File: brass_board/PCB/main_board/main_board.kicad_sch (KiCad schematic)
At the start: 133 parts

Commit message: Added LTspice tests and fixed error on opamp. ready for routing
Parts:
- A1: value (none) -> Arduino_Nano_v3.x; footprint (none) -> Module:Arduino_Nano
- C1, C10, C11, C12, C13, C2, C3, C4, C5, C6, C7, C8, C9: value (none) -> C_Small; footprint (none) -> Capacitor_SMD:C_0603_1608Metric
- C14, C15: renamed from C?; value (none) -> 100uF; footprint (none) -> Capacitor_SMD:C_1210_3225Metric
- FB1, FB2, FB3: value (none) -> FerriteBead_Small; footprint (none) -> Resistor_SMD:R_0805_2012Metric
- J1, J15: value (none) -> Conn_POS_input_B; footprint (none) -> Connector_PinHeader_2.54mm:PinHeader_1x03_P2.54mm_Vertical
- J10, J26: value (none) -> Conn_Galvo_B; footprint (none) -> Connector_PinHeader_2.54mm:PinHeader_1x03_P2.54mm_Vertical
- J11: value (none) -> Conn_OLED; footprint (none) -> Connector_PinHeader_2.54mm:PinHeader_1x04_P2.54mm_Vertical
- J12: value (none) -> Conn_LED_CTL; footprint (none) -> Connector_PinHeader_2.54mm:PinHeader_1x02_P2.54mm_Vertical
- J13: value (none) -> Conn_Laser_Trigger; footprint (none) -> Connector_PinHeader_2.54mm:PinHeader_1x02_P2.54mm_Vertical
- J14, J2: value (none) -> Conn_POS_input_A; footprint (none) -> Connector_PinHeader_2.54mm:PinHeader_1x03_P2.54mm_Vertical
- J16, J17, J18, J21, J23, J24: value (none) -> Conn_02x02_Odd_Even; footprint (none) -> Connector_PinHeader_2.54mm:PinHeader_2x02_P2.54mm_Vertical
- J19: value (none) -> Conn_ADC; footprint (none) -> Connector_PinHeader_2.54mm:PinHeader_1x04_P2.54mm_Vertical
- J20, J6: value (none) -> Conn_DAC; footprint (none) -> Connector_PinHeader_2.54mm:PinHeader_1x03_P2.54mm_Vertical
- J22, J8: value (none) -> Conn_01x03_Male_Power; footprint (none) -> Connector_PinHeader_2.54mm:PinHeader_1x03_P2.54mm_Vertical
- J25, J9: value (none) -> Conn_Galvo_A; footprint (none) -> Connector_PinHeader_2.54mm:PinHeader_1x03_P2.54mm_Vertical
- J27, J3: value (none) -> Conn_01x40_Male; footprint (none) -> Connector_PinHeader_2.54mm:PinHeader_2x20_P2.54mm_Vertical
- J4: value (none) -> Conn_01x04_Male; footprint (none) -> Connector_PinHeader_2.54mm:PinHeader_1x04_P2.54mm_Vertical
- J5: value (none) -> Conn_ADC; footprint (none) -> Connector_PinHeader_2.54mm:PinHeader_2x02_P2.54mm_Vertical
- J7: value (none) -> Conn_LED_PWM; footprint (none) -> Connector_PinHeader_2.54mm:PinHeader_1x02_P2.54mm_Vertical
- Q1, Q2: value (none) -> MMBT3904; footprint (none) -> Package_TO_SOT_SMD:SOT-23
- R1, R13, R14, R2, R20, R21, R22, R23, R24, R25, R26, R27, R28, R29, R3, R30, R31, R32, R33, R34, R35, R36, R37, R4, R5, R6, R7, R8: value (none) -> 1k; footprint (none) -> Resistor_SMD:R_0603_1608Metric
- R10, R11, R12, R16, R17, R18, R19, R9: value (none) -> 12k; footprint (none) -> Resistor_SMD:R_0603_1608Metric
- R15: value (none) -> 5k; footprint (none) -> Resistor_SMD:R_0603_1608Metric
- R38, R39, R40, R41, R42, R43, R44, R45, R46, R47: value (none) -> R_Small_US; footprint (none) -> Resistor_SMD:R_0603_1608Metric
- RV1, RV10, RV11, RV12, RV2, RV3, RV4, RV5, RV6, RV7, RV8, RV9: value (none) -> 50k; footprint (none) -> Potentiometer_THT:Potentiometer_Bourns_3296W_Vertical
- TP1, TP2, TP3, TP4, TP5: value (none) -> TestPoint; footprint (none) -> Connector_PinHeader_2.54mm:PinHeader_1x01_P2.54mm_Vertical
- U1, U14, U2, U3, U4, U5, U6, U7: value (none) -> LM393; footprint (none) -> Package_SO:SOIC-8-1EP_3.9x4.9mm_P1.27mm_EP2.29x3mm
- U10, U11: value (none) -> Teensy4.0; footprint (none) -> teensy:Teensy40
- U12, U13, U15, U8, U9: value (none) -> TLV3201; footprint (none) -> Package_TO_SOT_SMD:SOT-23-5
- gave numbers to parts that had none: 6
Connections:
- net GND: now also R5.2, R7.2; no longer R6.2, R8.2
- net at R9.1, U6.1: now also R6.2; no longer R5.2
- net at R11.1, U6.7: now also R8.2; no longer R7.2
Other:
- note added: "MCU"
- moved on the sheet: A1, C1, C10, C11, C12, C13, C14, C15, C16, C17, C18, C19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

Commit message: RC1
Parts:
- removed A1: Arduino_Nano_v3.x, Module:Arduino_Nano, symbol MCU_Module:Arduino_Nano_v3.x
- removed Q1, Q2: MMBT3904, Package_TO_SOT_SMD:SOT-23, symbol Transistor_BJT:2N2219
- removed U15: TLV3201, Package_TO_SOT_SMD:SOT-23-5, symbol project:TLV3201
- added D1, D2, D3, D4, D5: (no value), symbol Device:LED
- added J28: (no value), symbol Connector:Conn_01x06_Male
- added Q1: (no value), symbol Transistor_BJT:MMBT3904
- added R56: (no value), symbol Device:R_Small_US
- added S1: (no value), symbol project:PTS525SM15SMTR2LFS
- added U15: (no value), symbol 74xx:74LS08
- added U16: (no value), symbol project:ARDUINO_PRO_MINI
- added U17: (no value), symbol project:74LVC1G34
- added U18: (no value), symbol Logic_LevelTranslator:TXS0102DCT
- C1, C12, C13, C2, C3, C4, C8, C9: value C_Small -> (none); footprint Capacitor_SMD:C_0603_1608Metric -> (none); LCSC (none) -> C57112
- C10, C11: value C_Small -> (none); footprint Capacitor_SMD:C_0603_1608Metric -> (none); LCSC (none) -> C15849
- C14, C15, C16, C17, C18, C19, C20, C21: value 100uF -> (none); footprint Capacitor_SMD:C_1210_3225Metric -> (none); LCSC (none) -> C90143
- C5: value C_Small -> (none); footprint Capacitor_SMD:C_0603_1608Metric -> (none); LCSC (none) -> C159797
- C6: value C_Small -> (none); footprint Capacitor_SMD:C_0603_1608Metric -> (none); LCSC (none) -> C1664
- C7: value C_Small -> (none); footprint Capacitor_SMD:C_0603_1608Metric -> (none); LCSC (none) -> C33353
- Cam_Input1: renamed from RV3; value 50k -> (none); footprint Potentiometer_THT:Potentiometer_Bourns_3296W_Vertical -> (none); LCSC (none) -> C118911
- Cam_Output1: renamed from RV4; value 50k -> (none); footprint Potentiometer_THT:Potentiometer_Bourns_3296W_Vertical -> (none); LCSC (none) -> C118911
- FB1, FB2, FB3: value FerriteBead_Small -> (none); footprint Resistor_SMD:R_0805_2012Metric -> (none); LCSC (none) -> C2286
- GalvoA_Gain1: renamed from RV10; value 50k -> (none); footprint Potentiometer_THT:Potentiometer_Bourns_3296W_Vertical -> (none); LCSC (none) -> C118911
- GalvoA_Offset1: renamed from RV8; value 50k -> (none); footprint Potentiometer_THT:Potentiometer_Bourns_3296W_Vertical -> (none); LCSC (none) -> C118911
- GalvoB_Gain1: renamed from RV11; value 50k -> (none); footprint Potentiometer_THT:Potentiometer_Bourns_3296W_Vertical -> (none); LCSC (none) -> C118911
- GalvoB_Offset1: renamed from RV9; value 50k -> (none); footprint Potentiometer_THT:Potentiometer_Bourns_3296W_Vertical -> (none); LCSC (none) -> C118911
- InputA_Gain1: renamed from RV5; value 50k -> (none); footprint Potentiometer_THT:Potentiometer_Bourns_3296W_Vertical -> (none); LCSC (none) -> C118911
- InputA_offset1: renamed from RV1; value 50k -> (none); footprint Potentiometer_THT:Potentiometer_Bourns_3296W_Vertical -> (none); LCSC (none) -> C118911
- InputB_Gain1: renamed from RV6; value 50k -> (none); footprint Potentiometer_THT:Potentiometer_Bourns_3296W_Vertical -> (none); LCSC (none) -> C118911
- InputB_offset1: renamed from RV2; value 50k -> (none); footprint Potentiometer_THT:Potentiometer_Bourns_3296W_Vertical -> (none); LCSC (none) -> C118911
- J1, J15: value Conn_POS_input_B -> (none); footprint Connector_PinHeader_2.54mm:PinHeader_1x03_P2.54mm_Vertical -> (none); LCSC (none) -> C124376
- J10, J26: value Conn_Galvo_B -> (none); footprint Connector_PinHeader_2.54mm:PinHeader_1x03_P2.54mm_Vertical -> (none); LCSC (none) -> C124376
- J11: value Conn_OLED -> (none); footprint Connector_PinHeader_2.54mm:PinHeader_1x04_P2.54mm_Vertical -> (none); LCSC (none) -> C124378
- J12: value Conn_LED_CTL -> (none); footprint Connector_PinHeader_2.54mm:PinHeader_1x02_P2.54mm_Vertical -> (none); LCSC (none) -> C358684
- J13: value Conn_Laser_Trigger -> (none); footprint Connector_PinHeader_2.54mm:PinHeader_1x02_P2.54mm_Vertical -> (none); LCSC (none) -> C358684
- J14, J2: value Conn_POS_input_A -> (none); footprint Connector_PinHeader_2.54mm:PinHeader_1x03_P2.54mm_Vertical -> (none); LCSC (none) -> C124376
- J16, J17, J18, J21, J23, J24: value Conn_02x02_Odd_Even -> (none); footprint Connector_PinHeader_2.54mm:PinHeader_2x02_P2.54mm_Vertical -> (none); LCSC (none) -> C66690
- J19: value Conn_ADC -> (none); footprint Connector_PinHeader_2.54mm:PinHeader_1x04_P2.54mm_Vertical -> (none); LCSC (none) -> C124378
- J20, J6: value Conn_DAC -> (none); footprint Connector_PinHeader_2.54mm:PinHeader_1x03_P2.54mm_Vertical -> (none); LCSC (none) -> C124376
- J22, J8: value Conn_01x03_Male_Power -> (none); footprint Connector_PinHeader_2.54mm:PinHeader_1x03_P2.54mm_Vertical -> (none); LCSC (none) -> C124376
- J25, J9: value Conn_Galvo_A -> (none); footprint Connector_PinHeader_2.54mm:PinHeader_1x03_P2.54mm_Vertical -> (none); LCSC (none) -> C124376
- J27, J3: value Conn_01x40_Male -> (none); footprint Connector_PinHeader_2.54mm:PinHeader_2x20_P2.54mm_Vertical -> (none); LCSC (none) -> C124378
- J4: value Conn_01x04_Male -> (none); footprint Connector_PinHeader_2.54mm:PinHeader_1x04_P2.54mm_Vertical -> (none); LCSC (none) -> C124378
- J5: value Conn_ADC -> (none); footprint Connector_PinHeader_2.54mm:PinHeader_2x02_P2.54mm_Vertical -> (none); LCSC (none) -> C358684
- J7: value Conn_LED_PWM -> (none); footprint Connector_PinHeader_2.54mm:PinHeader_1x02_P2.54mm_Vertical -> (none); LCSC (none) -> C358684
- LED_Trigger1: renamed from RV7; value 50k -> (none); footprint Potentiometer_THT:Potentiometer_Bourns_3296W_Vertical -> (none); LCSC (none) -> C118911
- Prog1: renamed from RV12; value 50k -> (none); footprint Potentiometer_THT:Potentiometer_Bourns_3296W_Vertical -> (none); LCSC (none) -> C118911
- R1, R13, R14, R2, R20, R21, R22, R23, R24, R25, R26, R27, R28, R29, R3, R30, R31, R32, R33, R34, R35, R36, R37, R4, R5, R6, R7, R8: value 1k -> (none); footprint Resistor_SMD:R_0603_1608Metric -> (none); LCSC (none) -> C328340
- R10, R11, R12, R16, R17, R18, R19, R9: value 12k -> (none); footprint Resistor_SMD:R_0603_1608Metric -> (none); LCSC (none) -> C22790
- R15: value 5k -> (none); footprint Resistor_SMD:R_0603_1608Metric -> (none); LCSC (none) -> C23162
- R38: value R_Small_US -> (none); footprint Resistor_SMD:R_0603_1608Metric -> (none); LCSC (none) -> C23162
- R39: value R_Small_US -> (none); footprint Resistor_SMD:R_0603_1608Metric -> (none); LCSC (none) -> C22790
- R40: value R_Small_US -> (none); footprint Resistor_SMD:R_0603_1608Metric -> (none); LCSC (none) -> C25805
- R41: value R_Small_US -> (none); footprint Resistor_SMD:R_0603_1608Metric -> (none); LCSC (none) -> C23147
- R42: value R_Small_US -> (none); footprint Resistor_SMD:R_0603_1608Metric -> (none); LCSC (none) -> C25957
- R43: value R_Small_US -> (none); footprint Resistor_SMD:R_0603_1608Metric -> (none); LCSC (none) -> C22947
- R44, R45, R46, R47: value R_Small_US -> (none); footprint Resistor_SMD:R_0603_1608Metric -> (none); LCSC (none) -> C22962
- TP1, TP2, TP3, TP4, TP5: value TestPoint -> (none); footprint Connector_PinHeader_2.54mm:PinHeader_1x01_P2.54mm_Vertical -> (none); LCSC (none) -> C81276
- U1, U14, U2, U3, U4, U5, U6, U7: value LM393 -> (none); footprint Package_SO:SOIC-8-1EP_3.9x4.9mm_P1.27mm_EP2.29x3mm -> (none); LCSC (none) -> C9418
- U10, U11: value Teensy4.0 -> (none); footprint teensy:Teensy40 -> (none)
- U12, U13, U8, U9: value TLV3201 -> (none); footprint Package_TO_SOT_SMD:SOT-23-5 -> (none); LCSC (none) -> C105188
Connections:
- net +3V3: now also J28.4 (Pin_4), U15.14 (VCC), U16.JP1_4 (VCC), U16.JP6_4 (VCC_1), U18.3 (VCCA), U18.6 (OE)
- net +5V: now also U17.5 (VCC), U18.7 (VCCB); no longer R45.1, R46.1, U11.33 (VIN)
- net GND: now also U14.5 (+), D1.1 (K), D2.1 (K), D3.1 (K), D4.1 (K), D5.1 (K), J28.5 (Pin_5), J28.6 (Pin_6), Q1.2 (E), S1.1, S1.2, U15.10, U15.12, U15.13, U15.7 (GND), U15.9, U16.JP1_5 (GND), U16.JP1_6 (GND), U16.JP6_2 (GND_1), U16.JP7_9 (GND_2), U17.3 (GND), U18.2 (GND); no longer R47.2
- net LED_trigger: now also U12.1 (-); no longer U12.3 (+)
- net PWM_DAC: no longer U11.4 (2_OUT2)
- net Cam_In: now reaches J4.4 (Pin_4), TP1.1, U8.4
- net at U11.10 (8_TX2_IN1): no longer U10.10 (8_TX2_IN1)
- net at U10.11 (9_OUT1C): no longer U11.11 (9_OUT1C)
- net at J27.24 (Pin_24), J3.24 (Pin_24), U10.12 (10_CS_MQSR): no longer U11.12 (10_CS_MQSR)
- net at J27.21 (Pin_21), J3.21 (Pin_21), U10.13 (11_MOSI_CTX1): no longer U11.13 (11_MOSI_CTX1)
- net at J27.19 (Pin_19), J3.19 (Pin_19), U10.14 (12_MISO_MQSL): no longer U11.14 (12_MISO_MQSL)
- net at U10.15 (VBAT): no longer U11.15 (VBAT)
- net at U10.16 (3V3): no longer U11.16 (3V3)
- net at U10.18 (PROGRAM): now also Q1.3 (C); no longer U11.18 (PROGRAM)
- net at U10.19 (ON_OFF): no longer U11.19 (ON_OFF)
- net at U10.2 (0_RX1_CRX2_CS1): no longer U11.2 (0_RX1_CRX2_CS1)
- net at J27.23 (Pin_23), J3.23 (Pin_23), U10.20 (13_SCK_CRX1_LED): no longer U11.20 (13_SCK_CRX1_LED)
- net at U10.21 (14_A0_TX3_SPDIF_OUT): no longer U11.21 (14_A0_TX3_SPDIF_OUT)
- net at U11.23 (16_A2_RX4_SCL1): no longer U10.23 (16_A2_RX4_SCL1)
- net at U11.24 (17_A3_TX4_SDA1): no longer U10.24 (17_A3_TX4_SDA1)
- net SGT_SDA: now reaches U10.25 (18_A4_SDA0), U11.25 (18_A4_SDA0)
- net SGT_SCL: now reaches U10.26 (19_A5_SCL0), U11.26 (19_A5_SCL0)
- net SGT_LRCLK: now reaches U10.27 (20_A6_TX5_LRCLK1), U11.27 (20_A6_TX5_LRCLK1)
- net SGT_BCLK: now reaches U10.28 (21_A7_RX5_BCLK1), U11.28 (21_A7_RX5_BCLK1)
- net at U10.29 (22_A8_CTX1): no longer U11.29 (22_A8_CTX1)
- net at U10.3 (1_TX1_CTX2_MISO1): no longer U11.3 (1_TX1_CTX2_MISO1)
- net SGT_MCLK: now reaches U10.30 (23_A9_CRX1_MCLK1), U11.30 (23_A9_CRX1_MCLK1)
- net SGT_3.3: now reaches U10.31 (3V3), U11.31 (3V3)
- net at U10.34 (VUSB): no longer U11.34 (VUSB)
- net at U10.35 (24_A10_TX6_SCL2): no longer U11.35 (24_A10_TX6_SCL2)
- net at U10.36 (25_A11_RX6_SDA2): no longer U11.36 (25_A11_RX6_SDA2)
- net at U10.37 (26_A12_MOSI1): no longer U11.37 (26_A12_MOSI1)
- net at U10.38 (27_A13_SCK1): no longer U11.38 (27_A13_SCK1)
- net at U10.39 (28_RX7): no longer U11.39 (28_RX7)
- net at U10.40 (29_TX7): no longer U11.40 (29_TX7)
- net at U10.41 (30_CRX3): no longer U11.41 (30_CRX3)
- net at U10.42 (31_CTX3): no longer U11.42 (31_CTX3)
- net at U10.43 (32_OUT1B): no longer U11.43 (32_OUT1B)
- net at U10.44 (33_MCLK2): no longer U11.44 (33_MCLK2)
- net at U10.45 (34_DAT1_MISO2): no longer U11.45 (34_DAT1_MISO2)
- net at U10.46 (35_DAT0_MOSI2): no longer U11.46 (35_DAT0_MOSI2)
- net at U10.48 (36_CLK_CS2): no longer U11.48 (36_CLK_CS2)
- net at U10.49 (3V3): no longer U11.49 (3V3)
- net at J27.15 (Pin_15), J3.15 (Pin_15), U10.5 (3_LRCLK2)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: no longer U11.5 (3_LRCLK2)
- net at U10.50 (37_CMD_SCK2): no longer U11.50 (37_CMD_SCK2)
- net at U10.51 (38_DAT3_RX5): no longer U11.51 (38_DAT3_RX5)
- net at U10.52 (39_DAT2_TX5): no longer U11.52 (39_DAT2_TX5)
- net at U10.53 (D-): no longer U11.53 (D-)
- net at U10.54 (D+): no longer U11.54 (D+)
- net at J27.7 (Pin_7), J3.7 (Pin_7), U10.6 (4_BCLK2)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: no longer U11.6 (4_BCLK2)
- net at J27.32 (Pin_32), J3.32 (Pin_32), U10.7 (5_IN2): no longer U11.7 (5_IN2)
- net at J27.33 (Pin_33), J3.33 (Pin_33), U10.8 (6_OUT1D): no longer U11.8 (6_OUT1D)
- net at U11.9 (7_RX2_OUT1A): no longer U10.9 (7_RX2_OUT1A)
- net Clear_Fault: now reaches R45.2
- net Clear_Fault: now also U10.23 (16_A2_RX4_SCL1), S1.3, S1.4, U16.JP7_5 (D5)
- net at U14.6 (_): now also U14.7
- net at R47.1: now also D5.2 (A); no longer R46.2
- net at R44.2: now also U15.3, U18.5 (A1)
- net Prog_Reset: now reaches J27.29 (Pin_29), J3.29 (Pin_29), U13.3 (+)
- net Veapons Hot: now reaches J27.31 (Pin_31), J3.31 (Pin_31)
- net Veapons Hot: now also U15.1
- net at LED_Trigger1.2: now also U12.3 (+); no longer U12.1 (-)
- net at R38.2: now also Q1.1 (B)
- net at J13.1 (Pin_1): now also U17.4
- new net: D1.2 (A), R44.1
- new net: D4.2 (A), R46.1
- new net: U15.2, U15.6
- new net: D3.2 (A), R56.1
- new net: D2.2 (A), R45.1
- new net: U17.2, U18.8 (B1)
- new net: J28.1 (Pin_1), U16.JP1_1 (DTR)
- new net: J28.2 (Pin_2), U16.JP1_2 (TXO)
- new net: J28.3 (Pin_3), U16.JP1_3 (RXI)
- new net Fault: R47.2, U10.24 (17_A3_TX4_SDA1), U16.JP7_7 (D3)
- new net LAZOR!!!: R46.2, U15.5, U16.JP7_6 (D4)
- new net LAZOR?: R56.2, U10.22 (15_A1_RX3_SPDIF_IN), U15.4, U16.JP7_8 (D2)
- new net SGT_RX: U10.10 (8_TX2_IN1), U11.12 (10_CS_MQSR)
- new net SGT_TX: U10.9 (7_RX2_OUT1A), U11.11 (9_OUT1C)
- now unconnected: U11.22 (15_A1_RX3_SPDIF_IN)
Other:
- note added: "Audio Board"
- note added: "Unused"
- moved on the sheet: C1, C10, C11, C12, C13, C14, C15, C16, C17, C18, C19, C2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

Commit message: Fixed Ferrite Bead
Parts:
- FB1, FB2, FB3: LCSC C2286 -> C1017
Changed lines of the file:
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@@
       (effects (font (size 1.27 1.27)) hide)
     )
-    (property "Datasheet" "https://datasheet.lcsc.com/lcsc/1810231112_Hubei-KENTO-Elec-KT-0603R_C2286.pdf" (id 3) (at 396.24 210.82 0)
+    (property "Datasheet" "" (id 3) (at 396.24 210.82 0)
       (effects (font (size 1.27 1.27)) hide)
     )
-    (property "LCSC" "C2286" (id 4) (at 396.24 210.82 0)
+    (property "LCSC" "C1017" (id 4) (at 396.24 210.82 0)
       (effects (font (size 1.27 1.27)) hide)
     )
@@
       (effects (font (size 1.27 1.27)) hide)
     )
-    (property "Datasheet" "https://datasheet.lcsc.com/lcsc/1810231112_Hubei-KENTO-Elec-KT-0603R_C2286.pdf" (id 3) (at 396.24 222.25 0)
+    (property "Datasheet" "" (id 3) (at 396.24 222.25 0)
       (effects (font (size 1.27 1.27)) hide)
     )
-    (property "LCSC" "C2286" (id 4) (at 396.24 222.25 0)
+    (property "LCSC" "C1017" (id 4) (at 396.24 222.25 0)
       (effects (font (size 1.27 1.27)) hide)
     )
@@
       (effects (font (size 1.27 1.27)) hide)
     )
-    (property "Datasheet" "https://datasheet.lcsc.com/lcsc/1810231112_Hubei-KENTO-Elec-KT-0603R_C2286.pdf" (id 3) (at 396.24 200.66 0)
+    (property "Datasheet" "" (id 3) (at 396.24 200.66 0)
       (effects (font (size 1.27 1.27)) hide)
     )
-    (property "LCSC" "C2286" (id 4) (at 396.24 200.66 0)
+    (property "LCSC" "C1017" (id 4) (at 396.24 200.66 0)
       (effects (font (size 1.27 1.27)) hide)
     )
@@
     )
     (path "/a4b589db-0333-4020-beb7-903028d7dbe2"
-      (reference "FB1") (unit 1) (value "FerriteBead_Small") (footprint "Resistor_SMD:R_0805_2012Metric")
+      (reference "FB1") (unit 1) (value "GZ2012D601TF") (footprint "Resistor_SMD:R_0805_2012Metric")
     )
     (path "/4979cd09-d197-451f-afe9-7c58fc4156eb"
-      (reference "FB2") (unit 1) (value "FerriteBead_Small") (footprint "Resistor_SMD:R_0805_2012Metric")
+      (reference "FB2") (unit 1) (value "GZ2012D601TF") (footprint "Resistor_SMD:R_0805_2012Metric")
     )
     (path "/a3930b8d-8f0d-4e14-b54e-ccfff24a4ab2"
-      (reference "FB3") (unit 1) (value "FerriteBead_Small") (footprint "Resistor_SMD:R_0805_2012Metric")
+      (reference "FB3") (unit 1) (value "GZ2012D601TF") (footprint "Resistor_SMD:R_0805_2012Metric")
     )
     (path "/dd9eb4ec-d40e-4a5f-ae01-8b1070209db1"

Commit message: Sent to Fab
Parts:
- J11: LCSC C124378 -> (none)
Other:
- moved on the sheet: C18, C19, C3, C4, FB1, FB2, FB3, J22, J8, U1C, U4C, U5C

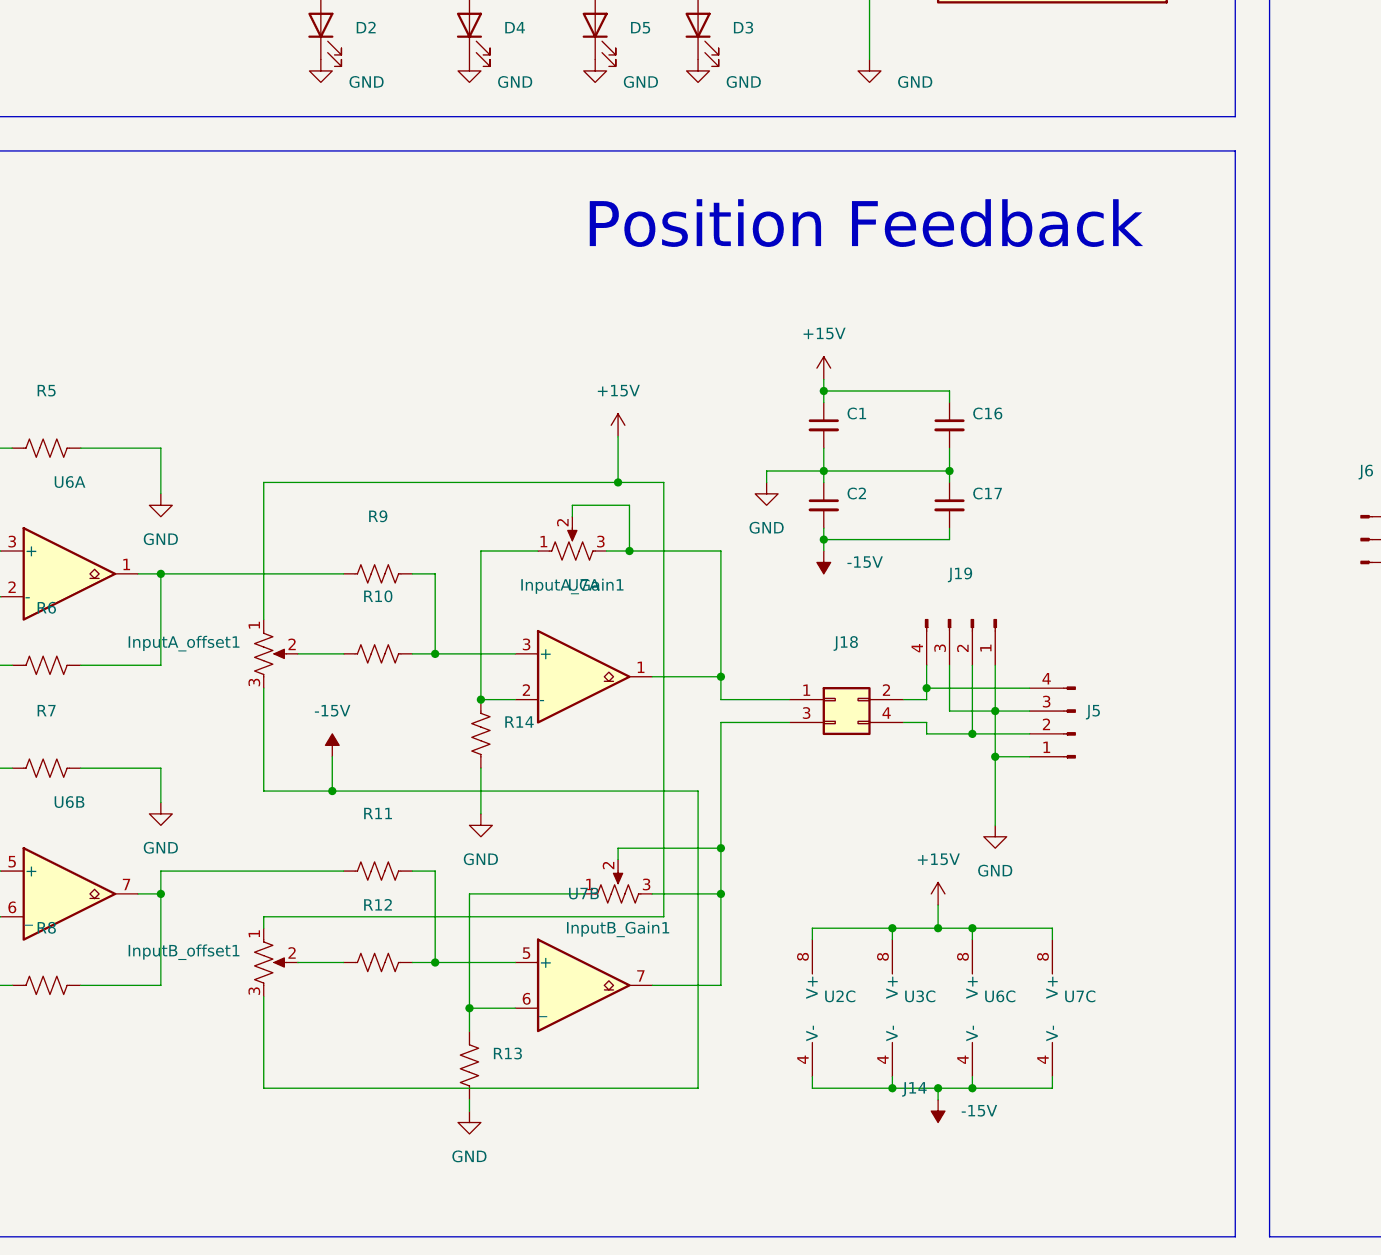
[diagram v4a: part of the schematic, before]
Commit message: Fixed driver footprint and parts errors:  now at Rev1
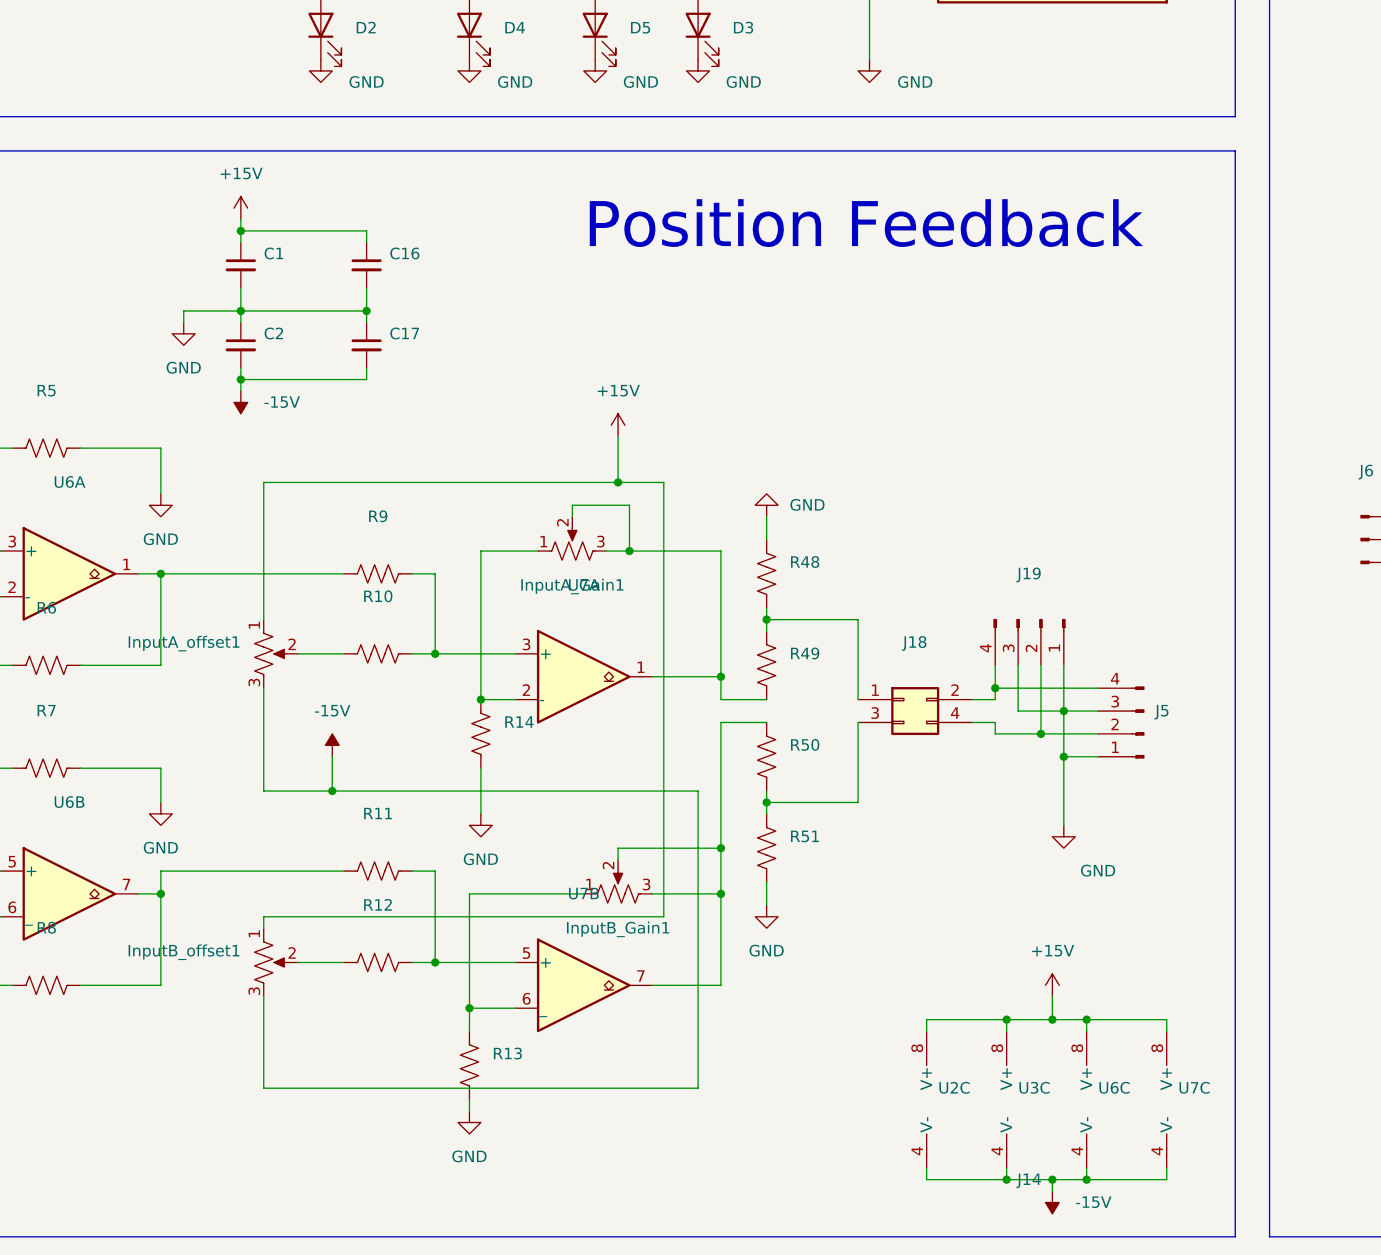
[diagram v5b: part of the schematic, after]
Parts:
- added R48, R49, R50, R51: (no value), symbol Device:R_US
- J27, J3: LCSC C124378 -> C124383
- J5: LCSC C358684 -> C66690
- R1, R13, R14, R2, R20, R21, R22, R23, R24, R25, R26, R27, R28, R29, R3, R30, R31, R32, R33, R34, R35, R36, R37, R4, R5, R6, R7, R8: LCSC C328340 -> C21190
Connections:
- net GND: now also R48.1, R51.2
- net at InputA_Gain1.2, InputA_Gain1.3, U7.1: now also R49.2; no longer J18.1 (Pin_1)
- net at InputB_Gain1.2, InputB_Gain1.3, U7.7: now also R50.1; no longer J18.3 (Pin_3)
- new net: J18.3 (Pin_3), R50.2, R51.1
- new net: J18.1 (Pin_1), R48.2, R49.1
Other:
- moved on the sheet: C1, C16, C17, C2, J18, J19, J5, U2C, U3C, U6C, U7C
